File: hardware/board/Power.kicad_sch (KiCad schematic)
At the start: 40 parts

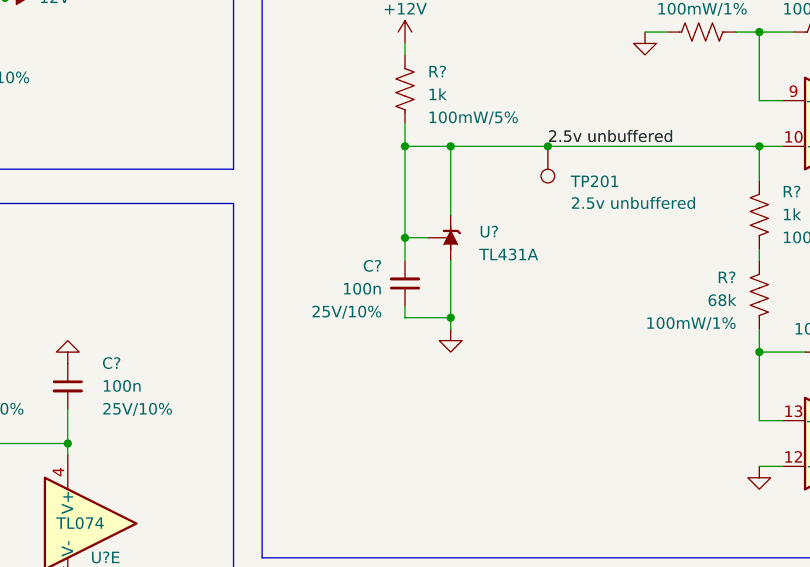
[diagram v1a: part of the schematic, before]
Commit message: Updated PCB to add and routed new components.
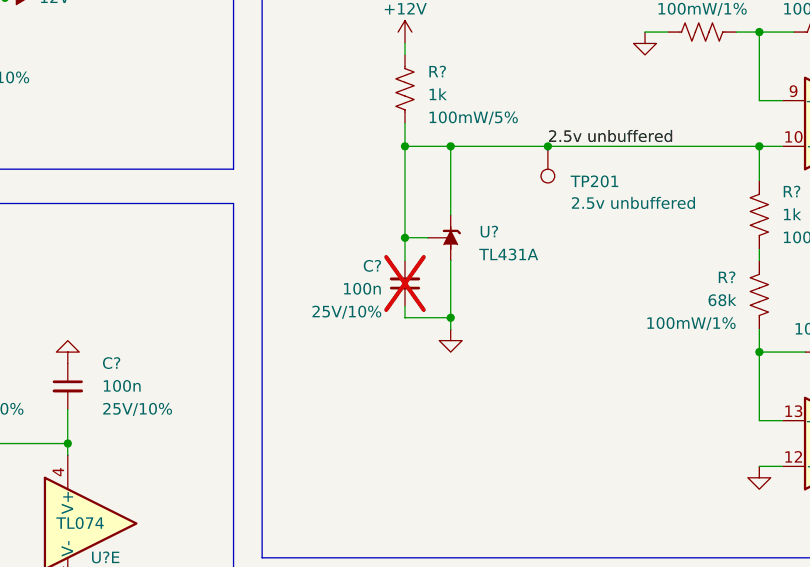
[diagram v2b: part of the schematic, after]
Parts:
- C?: now not fitted
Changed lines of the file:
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@@
   (title_block
     (title "Neptune")
-    (date "2023-07-20")
+    (date "2023-09-26")
     (rev "v0")
     (company "Winterbloom")
@@
   )
   (symbol (lib_id "Device:C_Small") (at 177.165 75.565 0) (mirror x) (unit 1)
-    (in_bom yes) (on_board yes) (dnp no)
+    (in_bom yes) (on_board yes) (dnp yes)
     (property "Reference" "C?" (at 174.625 73.6536 0)
       (effects (font (size 1.27 1.27)) (justify right))

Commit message: Lots of various small changes after reviewing the checklist.
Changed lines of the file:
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@@
   (title_block
     (title "Neptune")
-    (date "2023-09-26")
-    (rev "v0")
+    (date "2023-10-10")
+    (rev "v1")
     (company "Winterbloom")
     (comment 1 "Carson Walls")
@@
   )
   (symbol (lib_id "Device:C_Small") (at 105.41 117.475 0) (mirror x) (unit 1)
-    (in_bom yes) (on_board yes) (dnp no)
+    (in_bom yes) (on_board yes) (dnp no) (fields_autoplaced)
     (property "Reference" "C?" (at 109.22 114.935 0)
       (effects (font (size 1.27 1.27)) (justify left))
@@
   )
   (symbol (lib_id "Device:C_Small") (at 139.7 117.475 0) (mirror x) (unit 1)
-    (in_bom yes) (on_board yes) (dnp no)
+    (in_bom yes) (on_board yes) (dnp no) (fields_autoplaced)
     (property "Reference" "C?" (at 143.51 114.935 0)
       (effects (font (size 1.27 1.27)) (justify left))
@@
   )
   (symbol (lib_id "Device:C_Small") (at 95.25 49.53 0) (unit 1)
-    (in_bom yes) (on_board yes) (dnp no)
-    (property "Reference" "C?" (at 99.06 47.6313 0)
-      (effects (font (size 1.27 1.27)) (justify left))
-    )
-    (property "Value" "10u" (at 98.425 50.1713 0)
+    (in_bom yes) (on_board yes) (dnp no) (fields_autoplaced)
+    (property "Reference" "C?" (at 97.79 47.6313 0)
+      (effects (font (size 1.27 1.27)) (justify left))
+    )
+    (property "Value" "10u" (at 97.79 50.1713 0)
       (effects (font (size 1.27 1.27)) (justify left))
     )
@@
       (effects (font (size 1.27 1.27)) hide)
     )
-    (property "Rating" "25V/10%" (at 98.425 52.7113 0)
+    (property "Rating" "25V/10%" (at 97.79 52.7113 0)
       (effects (font (size 1.27 1.27)) (justify left))
     )
@@
   )
   (symbol (lib_id "Device:C_Small") (at 53.34 86.995 0) (mirror y) (unit 1)
-    (in_bom yes) (on_board yes) (dnp no)
+    (in_bom yes) (on_board yes) (dnp no) (fields_autoplaced)
     (property "Reference" "C?" (at 57.15 84.455 0)
       (effects (font (size 1.27 1.27)) (justify right))
@@
   )
   (symbol (lib_id "Device:C_Small") (at 88.9 86.995 0) (mirror y) (unit 1)
-    (in_bom yes) (on_board yes) (dnp no)
+    (in_bom yes) (on_board yes) (dnp no) (fields_autoplaced)
     (property "Reference" "C?" (at 92.71 84.455 0)
       (effects (font (size 1.27 1.27)) (justify right))
@@
   )
   (symbol (lib_id "Device:C_Small") (at 53.34 117.475 0) (mirror x) (unit 1)
-    (in_bom yes) (on_board yes) (dnp no)
+    (in_bom yes) (on_board yes) (dnp no) (fields_autoplaced)
     (property "Reference" "C?" (at 57.15 114.935 0)
       (effects (font (size 1.27 1.27)) (justify left))
@@
   (symbol (lib_id "Diode:1N5819") (at 71.12 40.005 180) (unit 1)
     (in_bom yes) (on_board yes) (dnp no) (fields_autoplaced)
-    (property "Reference" "D?" (at 71.4375 32.385 0)
+    (property "Reference" "D?" (at 71.4375 31.75 0)
       (effects (font (size 1.27 1.27)))
     )
-    (property "Value" "30V" (at 71.4375 34.925 0)
+    (property "Value" "30V" (at 71.4375 34.29 0)
       (effects (font (size 1.27 1.27)))
     )
@@
       (effects (font (size 1.27 1.27)) hide)
     )
-    (property "Rating" "500mA" (at 71.4375 37.465 0)
+    (property "Rating" "500mA" (at 71.4375 36.83 0)
       (effects (font (size 1.27 1.27)))
     )
@@
   )
   (symbol (lib_id "Device:C_Small") (at 139.7 86.995 0) (mirror y) (unit 1)
-    (in_bom yes) (on_board yes) (dnp no)
+    (in_bom yes) (on_board yes) (dnp no) (fields_autoplaced)
     (property "Reference" "C?" (at 143.51 84.455 0)
       (effects (font (size 1.27 1.27)) (justify right))
@@
   )
   (symbol (lib_id "Device:C_Small") (at 124.46 49.53 0) (unit 1)
-    (in_bom yes) (on_board yes) (dnp no)
-    (property "Reference" "C?" (at 128.27 47.6313 0)
-      (effects (font (size 1.27 1.27)) (justify left))
-    )
-    (property "Value" "10u" (at 127.635 50.1713 0)
+    (in_bom yes) (on_board yes) (dnp no) (fields_autoplaced)
+    (property "Reference" "C?" (at 127 47.6313 0)
+      (effects (font (size 1.27 1.27)) (justify left))
+    )
+    (property "Value" "10u" (at 127 50.1713 0)
       (effects (font (size 1.27 1.27)) (justify left))
     )
@@
       (effects (font (size 1.27 1.27)) hide)
     )
-    (property "Rating" "25V/10%" (at 127.635 52.7113 0)
+    (property "Rating" "25V/10%" (at 127 52.7113 0)
       (effects (font (size 1.27 1.27)) (justify left))
     )
@@
   )
   (symbol (lib_id "Device:C_Small") (at 123.19 117.475 0) (mirror x) (unit 1)
-    (in_bom yes) (on_board yes) (dnp no)
+    (in_bom yes) (on_board yes) (dnp no) (fields_autoplaced)
     (property "Reference" "C?" (at 127 114.935 0)
       (effects (font (size 1.27 1.27)) (justify left))
@@
   )
   (symbol (lib_id "Device:C_Small") (at 88.9 117.475 0) (mirror x) (unit 1)
-    (in_bom yes) (on_board yes) (dnp no)
+    (in_bom yes) (on_board yes) (dnp no) (fields_autoplaced)
     (property "Reference" "C?" (at 92.71 114.935 0)
       (effects (font (size 1.27 1.27)) (justify left))
@@
   )
   (symbol (lib_id "Device:C_Small") (at 71.12 86.995 0) (mirror y) (unit 1)
-    (in_bom yes) (on_board yes) (dnp no)
+    (in_bom yes) (on_board yes) (dnp no) (fields_autoplaced)
     (property "Reference" "C?" (at 74.93 84.455 0)
       (effects (font (size 1.27 1.27)) (justify right))
@@
   )
   (symbol (lib_id "Device:C_Small") (at 105.41 86.995 0) (mirror y) (unit 1)
-    (in_bom yes) (on_board yes) (dnp no)
+    (in_bom yes) (on_board yes) (dnp no) (fields_autoplaced)
     (property "Reference" "C?" (at 109.22 84.455 0)
       (effects (font (size 1.27 1.27)) (justify right))
@@
   )
   (symbol (lib_id "Device:C_Small") (at 71.12 117.475 0) (mirror x) (unit 1)
-    (in_bom yes) (on_board yes) (dnp no)
+    (in_bom yes) (on_board yes) (dnp no) (fields_autoplaced)
     (property "Reference" "C?" (at 74.93 114.935 0)
       (effects (font (size 1.27 1.27)) (justify left))
@@
   (symbol (lib_id "Device:FerriteBead_Small") (at 56.515 40.005 270) (unit 1)
     (in_bom yes) (on_board yes) (dnp no) (fields_autoplaced)
-    (property "Reference" "FB?" (at 56.5531 32.385 90)
+    (property "Reference" "FB?" (at 56.5531 31.75 90)
       (effects (font (size 1.27 1.27)))
     )
-    (property "Value" "1k @ 100MHz" (at 56.5531 34.925 90)
+    (property "Value" "1k @ 100MHz" (at 56.5531 34.29 90)
       (effects (font (size 1.27 1.27)))
     )
@@
       (effects (font (size 1.27 1.27)) hide)
     )
-    (property "Rating" "300mA" (at 56.5531 37.465 90)
+    (property "Rating" "300mA" (at 56.5531 36.83 90)
       (effects (font (size 1.27 1.27)))
     )
@@
   )
   (symbol (lib_id "winterbloom:TL074") (at 55.88 102.235 0) (unit 5)
-    (in_bom yes) (on_board yes) (dnp no)
+    (in_bom yes) (on_board yes) (dnp no) (fields_autoplaced)
     (property "Reference" "U?" (at 55.88 106.045 0)
       (effects (font (size 1.27 1.27)) (justify left))
@@
   )
   (symbol (lib_id "Device:C_Small") (at 123.19 86.995 0) (mirror y) (unit 1)
-    (in_bom yes) (on_board yes) (dnp no)
+    (in_bom yes) (on_board yes) (dnp no) (fields_autoplaced)
     (property "Reference" "C?" (at 127 84.455 0)
       (effects (font (size 1.27 1.27)) (justify right))

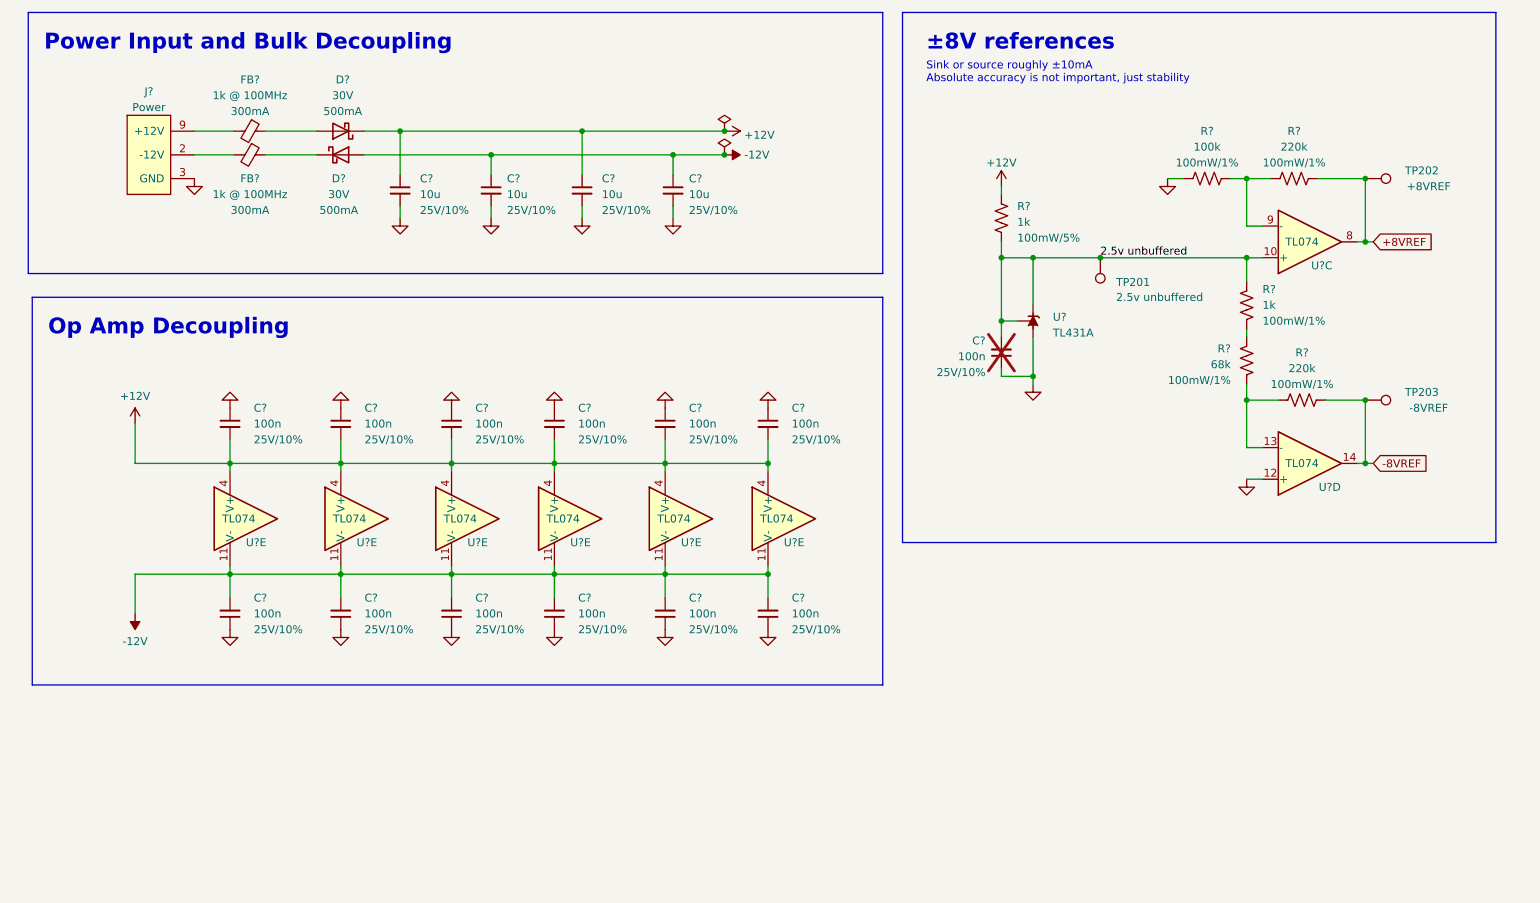
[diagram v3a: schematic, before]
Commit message: hardware: add MPNs, DigiKey part numbers, and LCSC part numbers for all BOM items
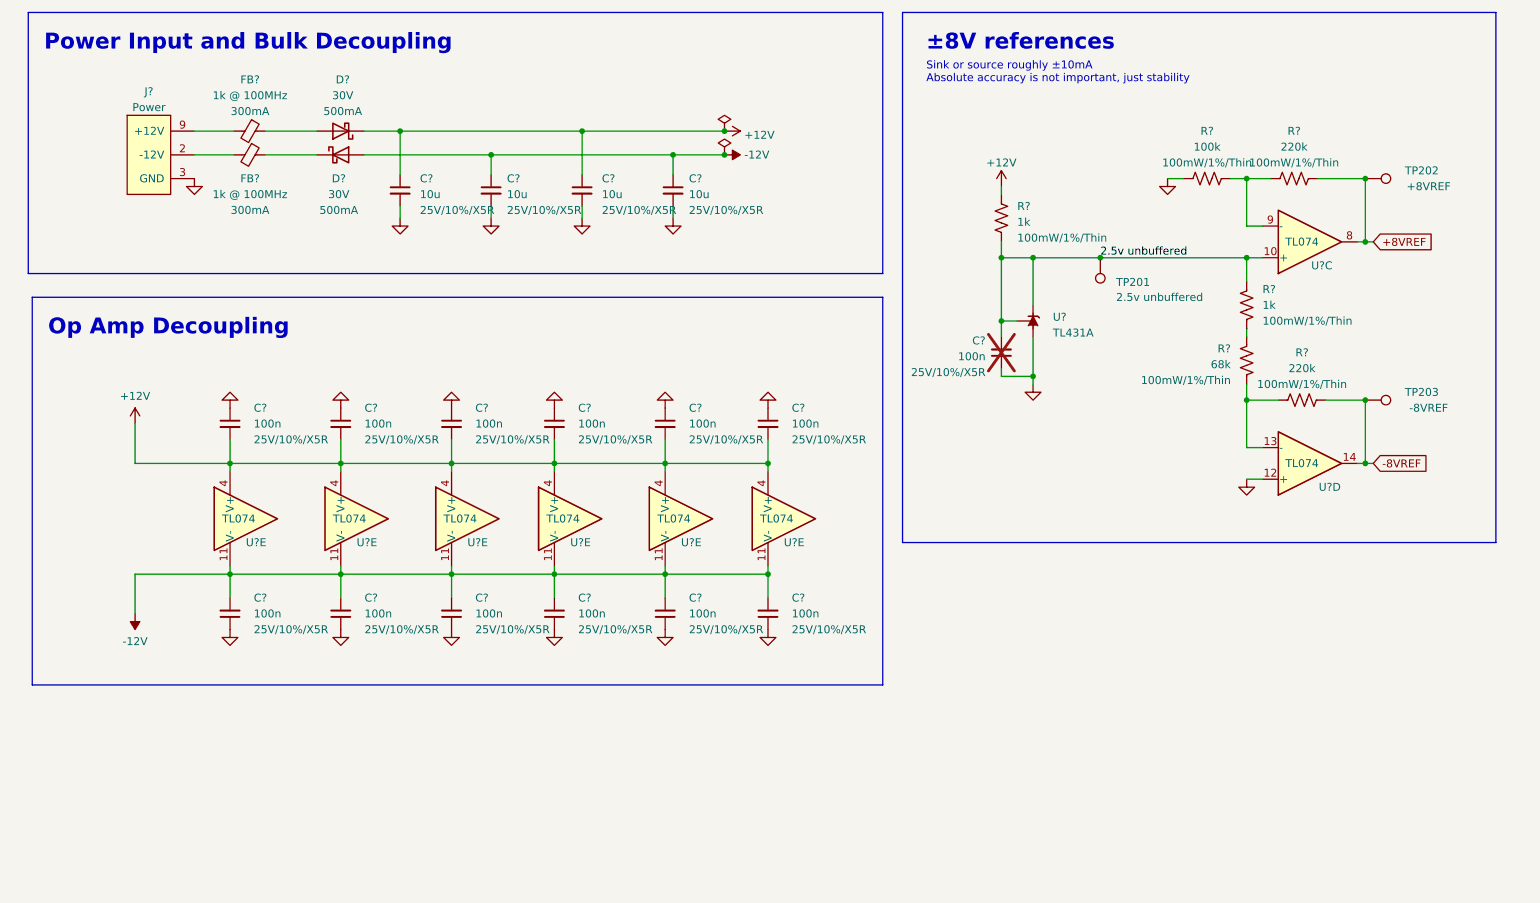
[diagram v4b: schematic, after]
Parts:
- C? (x4): DigiKey (none) -> 490-16824-1-ND; LCSC (none) -> C3909351; Rating 25V/10% -> 25V/10%/X5R; Substitutes Allowed (none) -> Yes
- C? (x13): DigiKey (none) -> 1276-1000-2-ND; LCSC (none) -> C1591; MPN C1608X7R1E104K080AA -> CL10B104KB8NNNC; Rating 25V/10% -> 25V/10%/X5R; Substitutes Allowed (none) -> Yes
- D? (x2): DigiKey (none) -> 1727-3876-1-ND; LCSC (none) -> C133636; MPN PMEG2005EGWX -> PMEG4005EH,115; Substitutes Allowed (none) -> Ask
- FB? (x2): DigiKey (none) -> 490-5212-1-ND; LCSC (none) -> C97851; MPN 742792664 -> BLM18BD121SN1D; Substitutes Allowed (none) -> Ask
- R?: DigiKey (none) -> YAG2323TR-ND; LCSC (none) -> C375503; MPN (none) -> RT0603FRE071KL; Rating 100mW/1% -> 100mW/1%/Thin; Substitutes Allowed (none) -> Yes
- R? (x2): DigiKey (none) -> YAG5946CT-ND; LCSC (none) -> C706140; MPN (none) -> RT0603FRE07220KL; Rating 100mW/1% -> 100mW/1%/Thin; Substitutes Allowed (none) -> Yes
- R?: DigiKey (none) -> YAG2323TR-ND; LCSC (none) -> C375503; MPN (none) -> RT0603FRE071KL; Rating 100mW/5% -> 100mW/1%/Thin; Substitutes Allowed (none) -> Yes
- R?: DigiKey (none) -> 13-RT0603FRE13100KLTR-ND; LCSC (none) -> C4107493; MPN (none) -> RT0603FRE13100KL; Rating 100mW/1% -> 100mW/1%/Thin; Substitutes Allowed (none) -> Yes
- R?: DigiKey (none) -> YAG5967CT-ND; LCSC (none) -> C706189; MPN (none) -> RT0603FRE0768KL; Rating 100mW/1% -> 100mW/1%/Thin; Substitutes Allowed (none) -> Yes
- U? (x8): DigiKey (none) -> 296-7198-1-ND; LCSC (none) -> C96507; MPN TL074CPW -> TL074CPWR; Substitutes Allowed (none) -> No
- U?: DigiKey (none) -> 1727-4260-1-ND; LCSC (none) -> C79737; Substitutes Allowed (none) -> No

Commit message: hardware: update schematic fonts/text sizes, some slight readability improvements
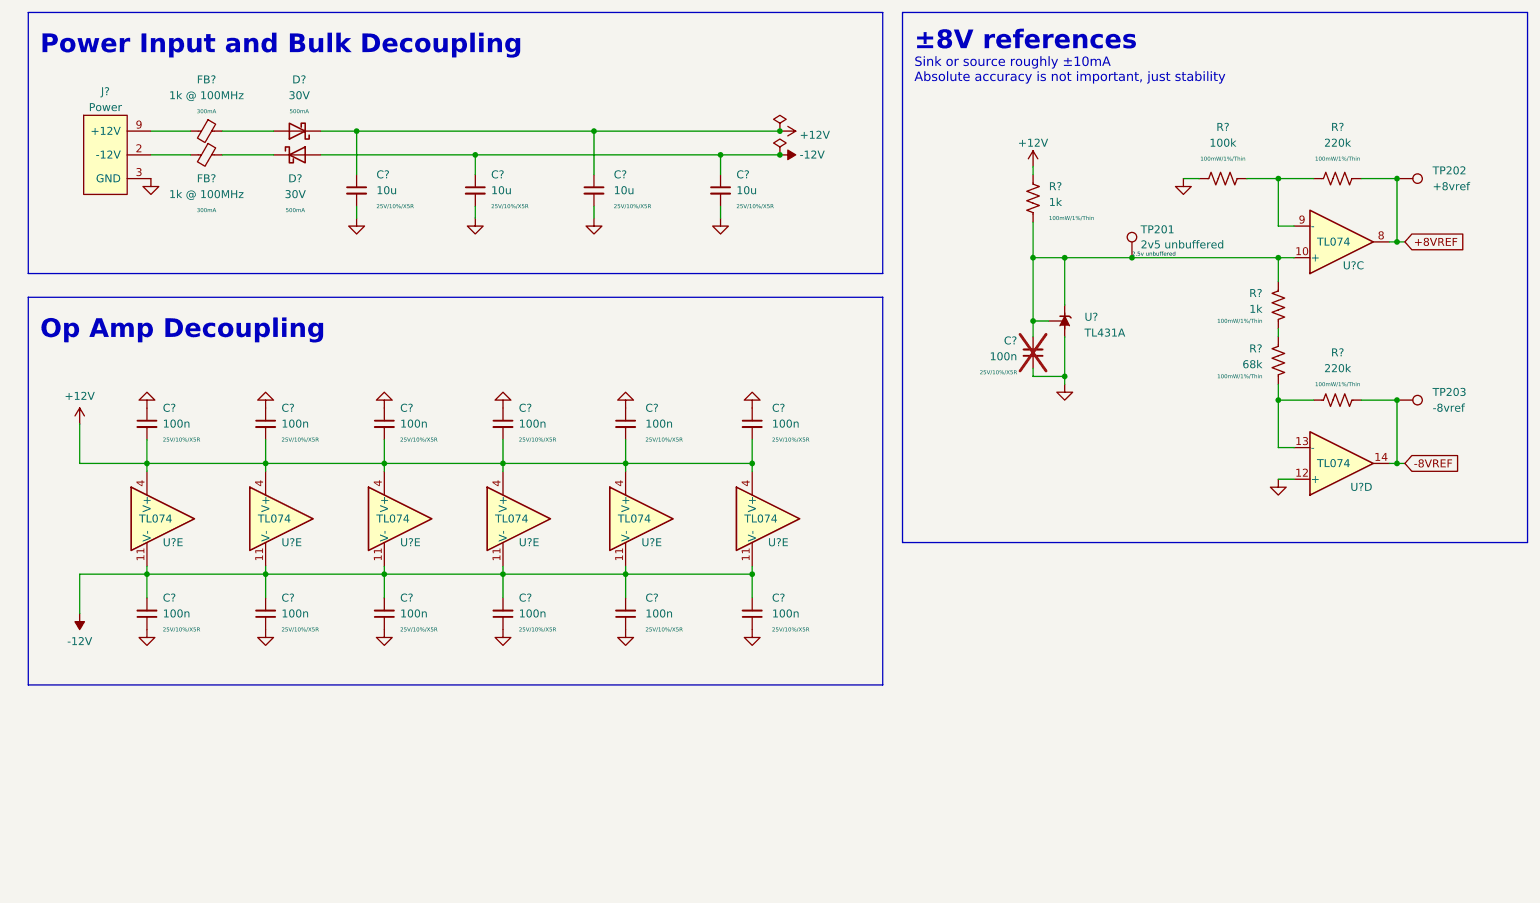
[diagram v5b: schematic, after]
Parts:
- TP201: Name 2.5v unbuffered -> 2v5 unbuffered
- TP202: Name +8VREF -> +8vref
- TP203: Name -8VREF -> -8vref
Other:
- moved on the sheet: C?, D?, FB?, J?, R?, TP201, TP202, TP203, U?, U?C, U?D, U?E
